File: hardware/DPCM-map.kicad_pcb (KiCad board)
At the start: 2 copper layers, 180 x 180 mm, 1 part

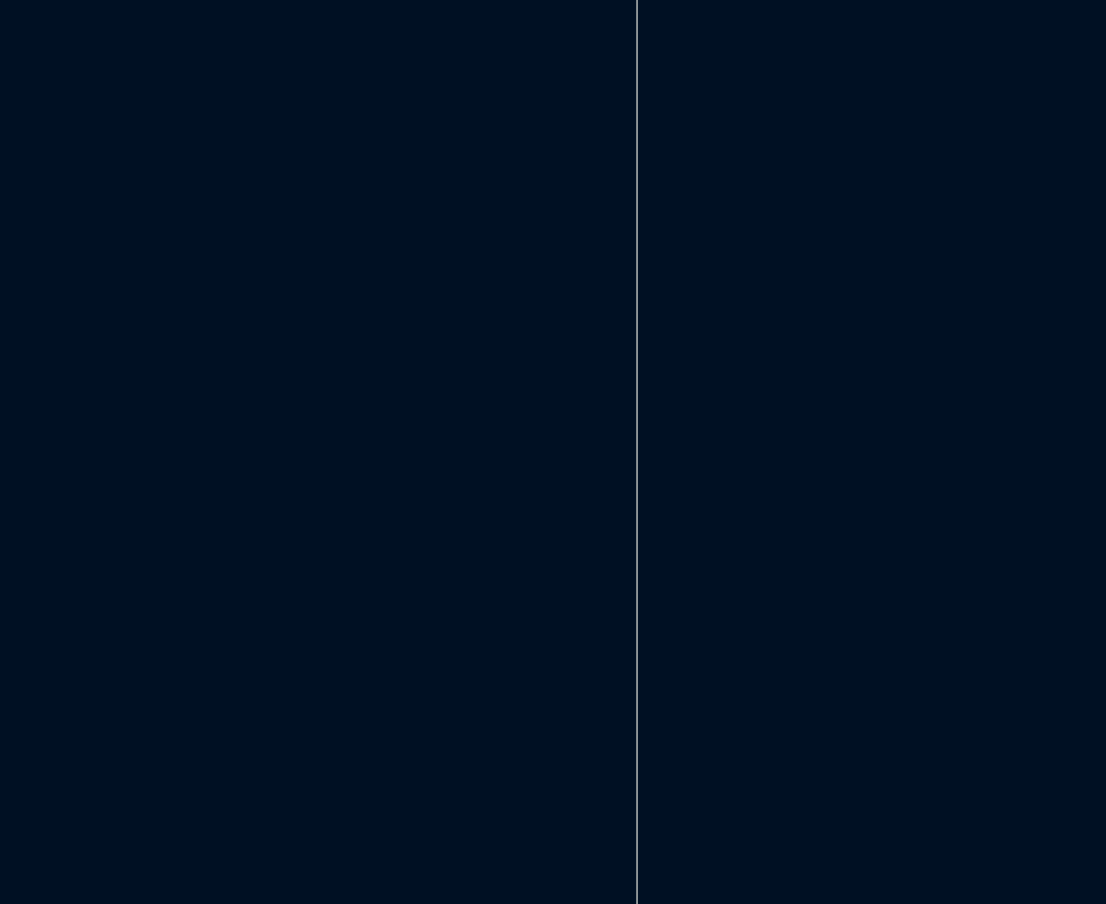
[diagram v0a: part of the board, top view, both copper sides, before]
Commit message: minor changes to pcb: added led footprint for comparison
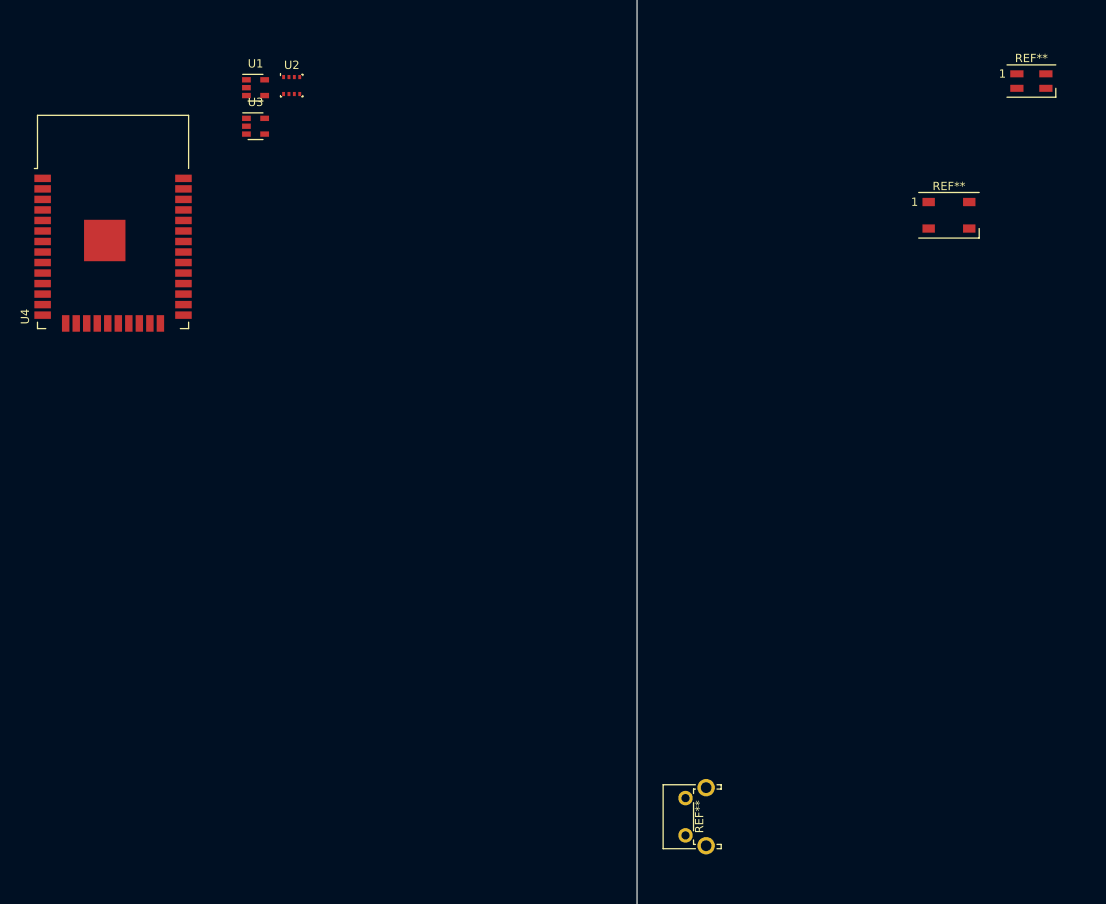
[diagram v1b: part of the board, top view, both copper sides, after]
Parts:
- added REF**: SW_Tactile_SPST_Angled_PTS645Vx39-2LFS, Button_Switch_THT:SW_Tactile_SPST_Angled_PTS645Vx39-2LFS, F.Cu at (5.85, 141.1)
- added REF**: LED_SK6812MINI_PLCC4_3.5x3.5mm_P1.75mm, LED_SMD:LED_SK6812MINI_PLCC4_3.5x3.5mm_P1.75mm, F.Cu at (47.6, 50.0)
- added REF**: LED_WS2812B_PLCC4_5.0x5.0mm_P3.2mm, LED_SMD:LED_WS2812B_PLCC4_5.0x5.0mm_P3.2mm, F.Cu at (37.6, 66.2)
- added U1: TLV75533PDBV, Package_TO_SOT_SMD:SOT-23-5, F.Cu at (-46.0, 50.9)
- added U2: BME280, Package_LGA:Bosch_LGA-8_2.5x2.5mm_P0.65mm_ClockwisePinNumbering, F.Cu at (-41.7, 50.6)
- added U3: MCP73811T, Package_TO_SOT_SMD:SOT-23-5, F.Cu at (-46.0, 55.5)
- added U4: ESP32-WROOM-32, RF_Module:ESP32-WROOM-32, F.Cu at (-63.2, 70.0)

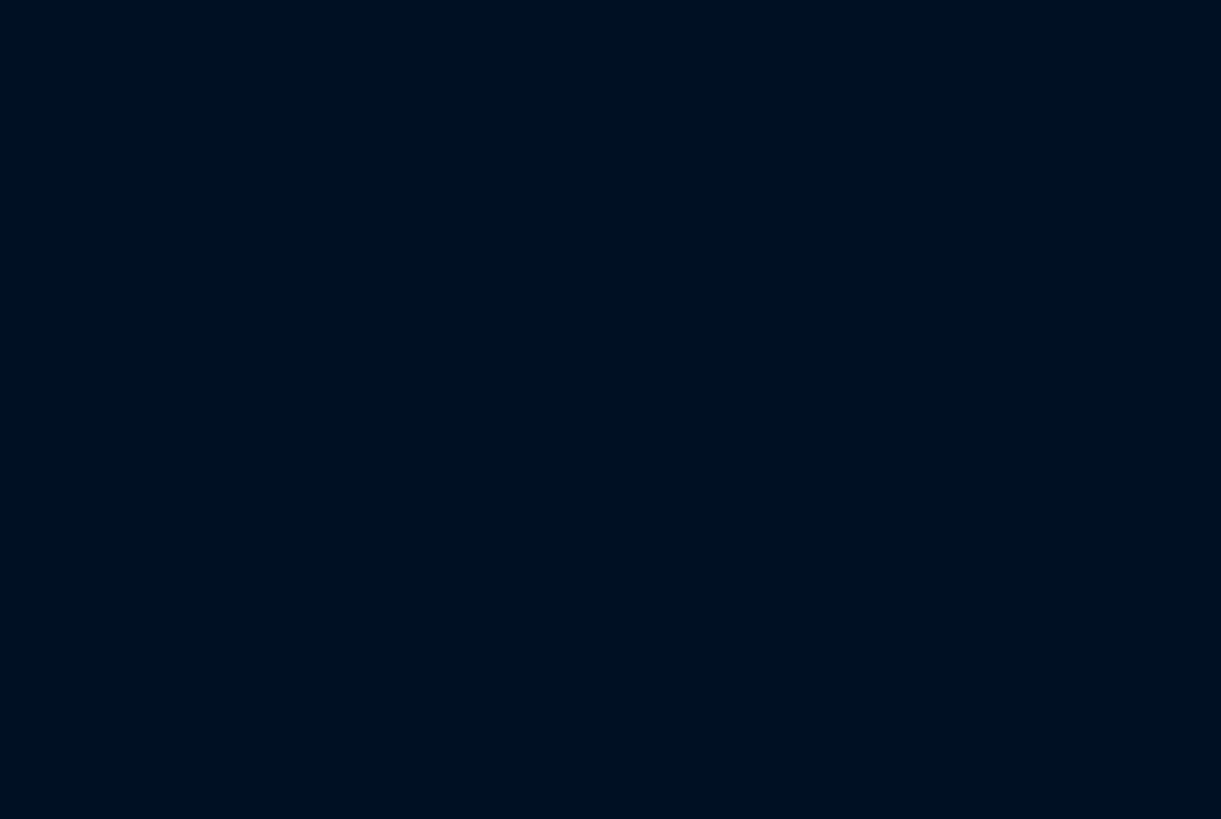
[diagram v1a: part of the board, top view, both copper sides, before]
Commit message: add LCSC ref
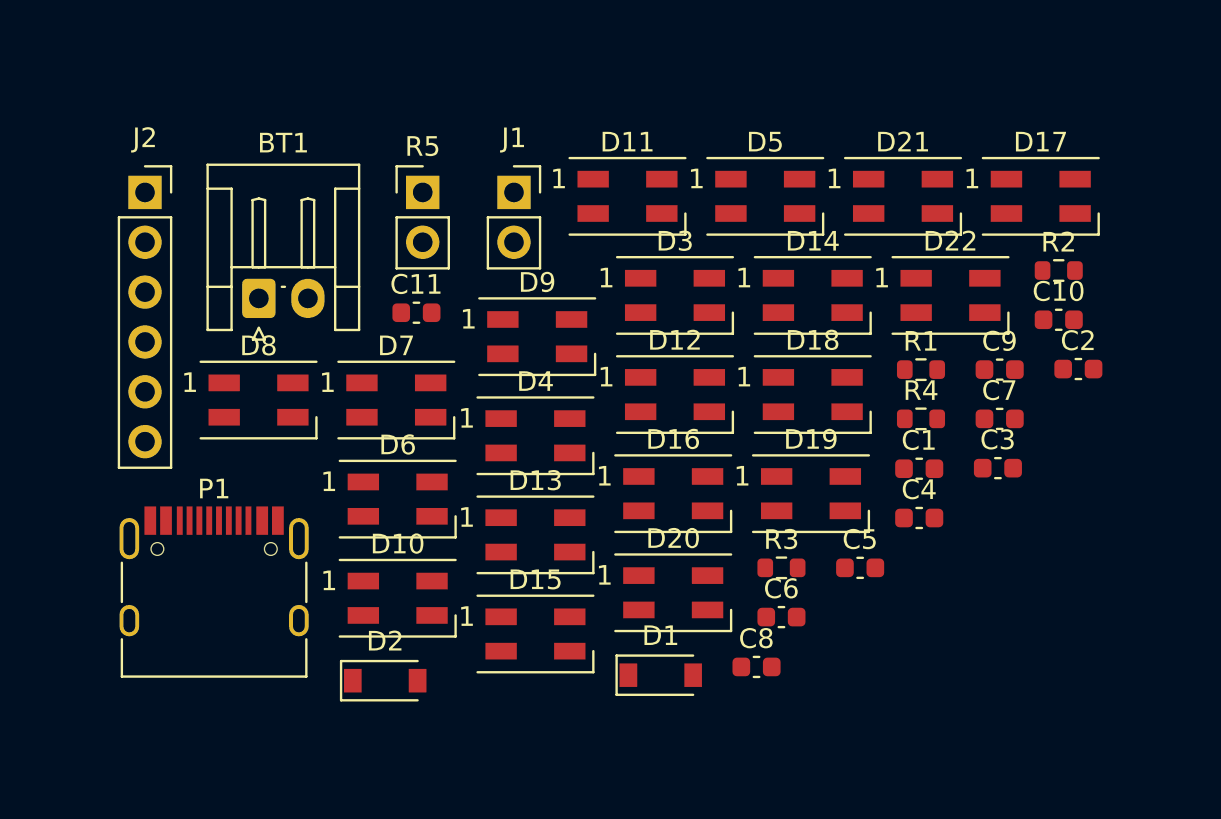
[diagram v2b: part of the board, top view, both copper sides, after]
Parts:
- added BT1: Battery_Cell, Connector_JST:JST_EH_S2B-EH_1x02_P2.50mm_Horizontal, F.Cu at (-52.4, 15.3)
- added C1: 10u, Capacitor_SMD:C_0603_1608Metric, F.Cu at (-18.7, 24.0)
- added C10: 10u, Capacitor_SMD:C_0603_1608Metric, F.Cu at (-11.6, 16.4)
- added C11: 0.1u, Capacitor_SMD:C_0603_1608Metric, F.Cu at (-44.4, 16.0)
- added C2: 1u, Capacitor_SMD:C_0603_1608Metric, F.Cu at (-10.6, 18.9)
- added C3: 10u, Capacitor_SMD:C_0603_1608Metric, F.Cu at (-14.7, 23.9)
- added C4: 0.1u, Capacitor_SMD:C_0603_1608Metric, F.Cu at (-18.7, 26.5)
- added C5: 10u, Capacitor_SMD:C_0603_1608Metric, F.Cu at (-21.8, 29.0)
- added C6: 10u, Capacitor_SMD:C_0603_1608Metric, F.Cu at (-25.8, 31.5)
- added C7: 0.1u, Capacitor_SMD:C_0603_1608Metric, F.Cu at (-14.6, 21.4)
- added C8: 10u, Capacitor_SMD:C_0603_1608Metric, F.Cu at (-27.0, 34.1)
- added C9: 10u, Capacitor_SMD:C_0603_1608Metric, F.Cu at (-14.6, 18.9)
- added D1: 1N5819, Diode_SMD:D_SOD-123, F.Cu at (-31.9, 34.5)
- added D10: WS2812B, LED_SMD:LED_SK6812MINI_PLCC4_3.5x3.5mm_P1.75mm, F.Cu at (-45.3, 30.6)
- added D11: WS2812B, LED_SMD:LED_SK6812MINI_PLCC4_3.5x3.5mm_P1.75mm, F.Cu at (-33.6, 10.1)
- added D12: WS2812B, LED_SMD:LED_SK6812MINI_PLCC4_3.5x3.5mm_P1.75mm, F.Cu at (-31.2, 20.2)
- added D13: WS2812B, LED_SMD:LED_SK6812MINI_PLCC4_3.5x3.5mm_P1.75mm, F.Cu at (-38.3, 27.4)
- added D14: WS2812B, LED_SMD:LED_SK6812MINI_PLCC4_3.5x3.5mm_P1.75mm, F.Cu at (-24.2, 15.2)
- added D15: WS2812B, LED_SMD:LED_SK6812MINI_PLCC4_3.5x3.5mm_P1.75mm, F.Cu at (-38.3, 32.4)
- added D16: WS2812B, LED_SMD:LED_SK6812MINI_PLCC4_3.5x3.5mm_P1.75mm, F.Cu at (-31.3, 25.2)
- added D17: WS2812B, LED_SMD:LED_SK6812MINI_PLCC4_3.5x3.5mm_P1.75mm, F.Cu at (-12.5, 10.1)
- added D18: WS2812B, LED_SMD:LED_SK6812MINI_PLCC4_3.5x3.5mm_P1.75mm, F.Cu at (-24.2, 20.2)
- added D19: WS2812B, LED_SMD:LED_SK6812MINI_PLCC4_3.5x3.5mm_P1.75mm, F.Cu at (-24.3, 25.2)
- added D2: 1N5819, Diode_SMD:D_SOD-123, F.Cu at (-46.0, 34.8)
- added D20: WS2812B, LED_SMD:LED_SK6812MINI_PLCC4_3.5x3.5mm_P1.75mm, F.Cu at (-31.3, 30.3)
- added D21: WS2812B, LED_SMD:LED_SK6812MINI_PLCC4_3.5x3.5mm_P1.75mm, F.Cu at (-19.6, 10.1)
- added D22: WS2812B, LED_SMD:LED_SK6812MINI_PLCC4_3.5x3.5mm_P1.75mm, F.Cu at (-17.1, 15.2)
- added D3: WS2812B, LED_SMD:LED_SK6812MINI_PLCC4_3.5x3.5mm_P1.75mm, F.Cu at (-31.2, 15.2)
- added D4: WS2812B, LED_SMD:LED_SK6812MINI_PLCC4_3.5x3.5mm_P1.75mm, F.Cu at (-38.3, 22.3)
- added D5: WS2812B, LED_SMD:LED_SK6812MINI_PLCC4_3.5x3.5mm_P1.75mm, F.Cu at (-26.6, 10.1)
- added D6: WS2812B, LED_SMD:LED_SK6812MINI_PLCC4_3.5x3.5mm_P1.75mm, F.Cu at (-45.3, 25.5)
- added D7: WS2812B, LED_SMD:LED_SK6812MINI_PLCC4_3.5x3.5mm_P1.75mm, F.Cu at (-45.4, 20.5)
- added D8: WS2812B, LED_SMD:LED_SK6812MINI_PLCC4_3.5x3.5mm_P1.75mm, F.Cu at (-52.4, 20.5)
- added D9: WS2812B, LED_SMD:LED_SK6812MINI_PLCC4_3.5x3.5mm_P1.75mm, F.Cu at (-38.2, 17.2)
- added J1: Conn_01x02_Male, Connector_PinSocket_2.54mm:PinSocket_1x02_P2.54mm_Vertical, F.Cu at (-39.4, 9.90)
- added J2: Conn_01x06_Male, Connector_PinSocket_2.54mm:PinSocket_1x06_P2.54mm_Vertical, F.Cu at (-58.2, 9.90)
- added P1: USB_C_Plug, Connector_USB:USB_C_Receptacle_HRO_TYPE-C-31-M-12, F.Cu at (-54.7, 30.7)
- added R1: 10k, Resistor_SMD:R_0603_1608Metric, F.Cu at (-18.6, 18.9)
- added R2: 10k, Resistor_SMD:R_0603_1608Metric, F.Cu at (-11.6, 13.9)
- added R3: 10k, Resistor_SMD:R_0603_1608Metric, F.Cu at (-25.8, 29.0)
- added R4: 10k, Resistor_SMD:R_0603_1608Metric, F.Cu at (-18.6, 21.4)
- added R5: LDR, Connector_PinHeader_2.54mm:PinHeader_1x02_P2.54mm_Vertical, F.Cu at (-44.0, 9.90)
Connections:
- U1 pad 4: Net-(U1-Pad4) -> (no net)
- U4 pad 10: Net-(U4-Pad10) -> (no net)
- U4 pad 11: Net-(U4-Pad11) -> (no net)
- U4 pad 12: Net-(U4-Pad12) -> (no net)
- U4 pad 13: Net-(U4-Pad13) -> (no net)
- U4 pad 14: Net-(U4-Pad14) -> (no net)
- U4 pad 16: Net-(U4-Pad16) -> (no net)
- U4 pad 17: Net-(U4-Pad17) -> (no net)
- U4 pad 18: Net-(U4-Pad18) -> (no net)
- U4 pad 19: Net-(U4-Pad19) -> (no net)
- U4 pad 20: Net-(U4-Pad20) -> (no net)
- U4 pad 21: Net-(U4-Pad21) -> (no net)
- U4 pad 22: Net-(U4-Pad22) -> (no net)
- U4 pad 24: Net-(U4-Pad24) -> (no net)
- U4 pad 25: Net-(U4-Pad25) -> (no net)
- U4 pad 26: Net-(U4-Pad26) -> (no net)
- U4 pad 27: Net-(U4-Pad27) -> (no net)
- U4 pad 28: Net-(U4-Pad28) -> (no net)
- U4 pad 29: Net-(U4-Pad29) -> (no net)
- U4 pad 30: Net-(U4-Pad30) -> (no net)
- U4 pad 31: Net-(U4-Pad31) -> (no net)
- U4 pad 32: Net-(U4-Pad32) -> (no net)
- U4 pad 37: Net-(U4-Pad37) -> (no net)
- U4 pad 4: Net-(U4-Pad4) -> (no net)
- U4 pad 5: Net-(U4-Pad5) -> (no net)
- U4 pad 6: Net-(U4-Pad6) -> (no net)
- U4 pad 8: Net-(U4-Pad8) -> (no net)
- U4 pad 9: Net-(U4-Pad9) -> (no net)

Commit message: add graphics,edges,keepout
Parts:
- removed the G*** at (180.0, 180.0)
- added G***: LOGO, map_edges_keepout:maps_edges_keepout, F.Cu at (288.8, 226.4)
- added REF**: MountingHole_4mm, MountingHole:MountingHole_4mm, F.Cu at (120.6, 58.5)
- added REF**: MountingHole_4mm, MountingHole:MountingHole_4mm, F.Cu at (120.6, 216.9)
- added REF**: MountingHole_4mm, MountingHole:MountingHole_4mm, F.Cu at (279.0, 216.9)
- added REF**: MountingHole_4mm, MountingHole:MountingHole_4mm, F.Cu at (279.0, 58.5)
- moved REF** 159.4 mm to (-77.9, -48.2)
- moved REF** 159.4 mm to (-87.9, -32.0)
- moved REF** 81.1 mm to (-71.2, 115.8)
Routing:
- added copper zone on B.Cu, net GND
- added copper zone on F.Cu, net GND
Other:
- board size 180 x 180 mm -> 177.4 x 177.4 mm

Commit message: cazzo commento a fare che tanto faremo il rebase
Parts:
- removed BT1: Battery_Cell, Connector_JST:JST_EH_S2B-EH_1x02_P2.50mm_Horizontal
- removed C1, C10, C3, C5, C6, C8, C9: 10u, Capacitor_SMD:C_0603_1608Metric
- removed C11, C4, C7: 0.1u, Capacitor_SMD:C_0603_1608Metric
- removed C2: 1u, Capacitor_SMD:C_0603_1608Metric
- removed D1, D2: 1N5819, Diode_SMD:D_SOD-123
- removed D10, D11, D12, D13, D14, D15, D16, D17, D18, D19, D20, D21, D22, D3, D4, D5, D6, D7, D8, D9: WS2812B, LED_SMD:LED_SK6812MINI_PLCC4_3.5x3.5mm_P1.75mm
- removed J1: Conn_01x02_Male, Connector_PinSocket_2.54mm:PinSocket_1x02_P2.54mm_Vertical
- removed J2: Conn_01x06_Male, Connector_PinSocket_2.54mm:PinSocket_1x06_P2.54mm_Vertical
- removed P1: USB_C_Plug, Connector_USB:USB_C_Receptacle_HRO_TYPE-C-31-M-12
- removed R1, R2, R3, R4: 10k, Resistor_SMD:R_0603_1608Metric
- removed R5: LDR, Connector_PinHeader_2.54mm:PinHeader_1x02_P2.54mm_Vertical
- removed the REF** at (-71.2, 115.8)
- removed the REF** at (-77.9, -48.2)
- removed the REF** at (-87.9, -32.0)
- removed U1: TLV75533PDBV, Package_TO_SOT_SMD:SOT-23-5
- removed U2: BME280, Package_LGA:Bosch_LGA-8_2.5x2.5mm_P0.65mm_ClockwisePinNumbering
- removed U3: MCP73811T, Package_TO_SOT_SMD:SOT-23-5
- removed U4: ESP32-WROOM-32, RF_Module:ESP32-WROOM-32

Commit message: first layout draft
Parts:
- removed the REF** at (120.6, 216.9)
- removed the REF** at (279.0, 216.9)
- removed the REF** at (279.0, 58.5)
- added C1: 10u, Capacitor_SMD:C_0603_1608Metric, F.Cu at (274.6, 123.4)
- added C10: 10u, Capacitor_SMD:C_0603_1608Metric, F.Cu at (273.5, 70.4)
- added C11: 100n, Capacitor_SMD:C_0603_1608Metric, F.Cu at (273.5, 73.6)
- added C12: 100n, Capacitor_SMD:C_0603_1608Metric, F.Cu at (268.8, 132.3)
- added C13: 100n, Capacitor_SMD:C_0603_1608Metric, F.Cu at (196.7, 122.6)
- added C14: 100n, Capacitor_SMD:C_0603_1608Metric, F.Cu at (273.5, 75.2)
- added C15: 18p, Capacitor_SMD:C_0805_2012Metric, F.Cu at (250.4, 110.9)
- added C16: 18p, Capacitor_SMD:C_0805_2012Metric, F.Cu at (249.6, 116.5)
- added C17: 10u, Capacitor_SMD:C_0603_1608Metric, F.Cu at (269.2, 116.0)
- added C18: 10u, Capacitor_SMD:C_0603_1608Metric, F.Cu at (255.3, 106.2)
- added C19: 100n, Capacitor_SMD:C_0603_1608Metric, F.Cu at (258.4, 106.2)
- added C2: 1u, Capacitor_SMD:C_0603_1608Metric, F.Cu at (277.2, 191.2)
- added C20: 100n, Capacitor_SMD:C_0603_1608Metric, F.Cu at (255.3, 104.6)
- added C21: 100n, Capacitor_SMD:C_0603_1608Metric, F.Cu at (189.6, 80.2)
- added C22: 100n, Capacitor_SMD:C_0603_1608Metric, F.Cu at (203.2, 72.2)
- added C23: 100n, Capacitor_SMD:C_0603_1608Metric, F.Cu at (183.0, 67.3)
- added C24: 100n, Capacitor_SMD:C_0603_1608Metric, F.Cu at (180.1, 97.0)
- added C25: 100n, Capacitor_SMD:C_0603_1608Metric, F.Cu at (237.9, 160.4)
- added C26: 100n, Capacitor_SMD:C_0603_1608Metric, F.Cu at (232.3, 145.6)
- added C27: 100n, Capacitor_SMD:C_0603_1608Metric, F.Cu at (213.9, 203.8)
- added C28: 100n, Capacitor_SMD:C_0603_1608Metric, F.Cu at (205.3, 116.3)
- added C29: 100n, Capacitor_SMD:C_0603_1608Metric, F.Cu at (274.6, 121.8)
- added C3: 10u, Capacitor_SMD:C_0603_1608Metric, F.Cu at (143.9, 90.9)
- added C30: 100n, Capacitor_SMD:C_0603_1608Metric, F.Cu at (181.6, 114.6)
- added C31: 100n, Capacitor_SMD:C_0603_1608Metric, F.Cu at (146.9, 103.9)
- added C32: 100n, Capacitor_SMD:C_0603_1608Metric, F.Cu at (160.9, 100.4)
- added C33: 100n, Capacitor_SMD:C_0603_1608Metric, F.Cu at (135.9, 81.6)
- added C34: 100n, Capacitor_SMD:C_0603_1608Metric, F.Cu at (274.6, 120.2)
- added C35: 100n, Capacitor_SMD:C_0603_1608Metric, F.Cu at (165.3, 80.2)
- added C36: 100n, Capacitor_SMD:C_0603_1608Metric, F.Cu at (242.8, 181.6)
- added C37: 100n, Capacitor_SMD:C_0603_1608Metric, F.Cu at (157.4, 167.5)
- added C38: 100n, Capacitor_SMD:C_0603_1608Metric, F.Cu at (218.7, 145.8)
- added C39: 100n, Capacitor_SMD:C_0603_1608Metric, F.Cu at (198.6, 139.1)
- added C4: 100n, Capacitor_SMD:C_0603_1608Metric, F.Cu at (277.2, 192.9)
- added C40: 100n, Capacitor_SMD:C_0603_1608Metric, F.Cu at (223.8, 153.5)
- added C5: 10u, Capacitor_SMD:C_0603_1608Metric, F.Cu at (268.8, 123.4)
- added C6: 10u, Capacitor_SMD:C_0603_1608Metric, F.Cu at (254.2, 159.5)
- added C7: 100n, Capacitor_SMD:C_0603_1608Metric, F.Cu at (269.2, 109.7)
- added C8: 10u, Capacitor_SMD:C_0603_1608Metric, F.Cu at (212.7, 133.1)
- added C9: 10u, Capacitor_SMD:C_0603_1608Metric, F.Cu at (273.5, 72.0)
- added D1: WS2812B, LED_SMD:LED_SK6812MINI_PLCC4_3.5x3.5mm_P1.75mm, F.Cu at (215.2, 206.7)
- added D10: WS2812B, LED_SMD:LED_SK6812MINI_PLCC4_3.5x3.5mm_P1.75mm, F.Cu at (255.9, 162.6)
- added D11: WS2812B, LED_SMD:LED_SK6812MINI_PLCC4_3.5x3.5mm_P1.75mm, F.Cu at (145.3, 94.1)
- added D12: WS2812B, LED_SMD:LED_SK6812MINI_PLCC4_3.5x3.5mm_P1.75mm, F.Cu at (239.4, 163.4)
- added D13: WS2812B, LED_SMD:LED_SK6812MINI_PLCC4_3.5x3.5mm_P1.75mm, F.Cu at (139.6, 81.6)
- added D14: WS2812B, LED_SMD:LED_SK6812MINI_PLCC4_3.5x3.5mm_P1.75mm, F.Cu at (148.2, 106.9)
- added D15: WS2812B, LED_SMD:LED_SK6812MINI_PLCC4_3.5x3.5mm_P1.75mm, F.Cu at (162.5, 103.3)
- added D16: WS2812B, LED_SMD:LED_SK6812MINI_PLCC4_3.5x3.5mm_P1.75mm, F.Cu at (181.4, 100.0)
- added D17: WS2812B, LED_SMD:LED_SK6812MINI_PLCC4_3.5x3.5mm_P1.75mm, F.Cu at (182.9, 117.4)
- added D18: WS2812B, LED_SMD:LED_SK6812MINI_PLCC4_3.5x3.5mm_P1.75mm, F.Cu at (206.6, 119.3)
- added D19: WS2812B, LED_SMD:LED_SK6812MINI_PLCC4_3.5x3.5mm_P1.75mm, F.Cu at (198.1, 125.6)
- added D2: WS2812B, LED_SMD:LED_SK6812MINI_PLCC4_3.5x3.5mm_P1.75mm, F.Cu at (244.1, 184.5)
- added D20: WS2812B, LED_SMD:LED_SK6812MINI_PLCC4_3.5x3.5mm_P1.75mm, F.Cu at (214.2, 136.1)
- added D21: WS2812B, LED_SMD:LED_SK6812MINI_PLCC4_3.5x3.5mm_P1.75mm, F.Cu at (199.9, 141.9)
- added D22: WS2812B, LED_SMD:LED_SK6812MINI_PLCC4_3.5x3.5mm_P1.75mm, F.Cu at (158.9, 170.5)
- added D23: 1N4148W, Diode_SMD:D_SOD-123, F.Cu at (218.8, 72.3)
- added D3: WS2812B, LED_SMD:LED_SK6812MINI_PLCC4_3.5x3.5mm_P1.75mm, F.Cu at (190.9, 83.1)
- added D4: WS2812B, LED_SMD:LED_SK6812MINI_PLCC4_3.5x3.5mm_P1.75mm, F.Cu at (225.1, 156.4)
- added D5: WS2812B, LED_SMD:LED_SK6812MINI_PLCC4_3.5x3.5mm_P1.75mm, F.Cu at (204.5, 75.1)
- added D6: WS2812B, LED_SMD:LED_SK6812MINI_PLCC4_3.5x3.5mm_P1.75mm, F.Cu at (222.4, 145.6)
- added D7: WS2812B, LED_SMD:LED_SK6812MINI_PLCC4_3.5x3.5mm_P1.75mm, F.Cu at (184.3, 70.1)
- added D8: WS2812B, LED_SMD:LED_SK6812MINI_PLCC4_3.5x3.5mm_P1.75mm, F.Cu at (233.7, 148.6)
- added D9: WS2812B, LED_SMD:LED_SK6812MINI_PLCC4_3.5x3.5mm_P1.75mm, F.Cu at (166.6, 83.0)
- added J1: JMP, Connector_PinSocket_2.54mm:PinSocket_1x02_P2.54mm_Vertical, F.Cu at (271.9, 106.9)
- added J2: Conn_01x06_Male, Connector_PinSocket_2.54mm:PinSocket_1x06_P2.54mm_Vertical, F.Cu at (258.5, 99.2)
- added J3: Touch_Pad_-, Connector_Wire:SolderWire-0.75sqmm_1x01_D1.25mm_OD2.3mm, F.Cu at (143.1, 58.4)
- added J4: Touch_Pad_0, Connector_Wire:SolderWire-0.75sqmm_1x01_D1.25mm_OD2.3mm, F.Cu at (143.1, 63.0)
- added J5: Touch_Pad_+, Connector_Wire:SolderWire-0.75sqmm_1x01_D1.25mm_OD2.3mm, F.Cu at (143.1, 67.9)
- added J6: JMP, Connector_PinSocket_2.54mm:PinSocket_1x02_P2.54mm_Vertical, F.Cu at (271.9, 113.1)
- added J7: SSD1306, Connector_PinHeader_2.54mm:PinHeader_1x04_P2.54mm_Vertical, F.Cu at (127.7, 110.8)
- added JP1: SolderJumper_3_Open, Jumper:SolderJumper-3_P1.3mm_Open_RoundedPad1.0x1.5mm_NumberLabels, F.Cu at (143.2, 118.8)
- added JP2: Jumper, Jumper:SolderJumper-2_P1.3mm_Bridged_RoundedPad1.0x1.5mm, F.Cu at (219.0, 74.8)
- added JP3: SolderJumper_3_Open, Jumper:SolderJumper-3_P1.3mm_Open_RoundedPad1.0x1.5mm_NumberLabels, F.Cu at (147.2, 118.6)
- added P1: USB_C_Plug, Connector_USB:USB_C_Receptacle_HRO_TYPE-C-31-M-12, F.Cu at (284.3, 126.8)
- added Q1: 2N7002, Package_TO_SOT_SMD:SOT-23, F.Cu at (262.5, 108.8)
- added Q2: 2N7002, Package_TO_SOT_SMD:SOT-23, F.Cu at (262.5, 115.6)
- added R1: 10k, Resistor_SMD:R_0603_1608Metric, F.Cu at (277.2, 199.4)
- added R2: 10k, Resistor_SMD:R_0603_1608Metric, F.Cu at (277.2, 197.7)
- added R3: 10k, Resistor_SMD:R_0603_1608Metric, F.Cu at (269.2, 106.6)
- added R4: 10k, Resistor_SMD:R_0603_1608Metric, F.Cu at (263.4, 59.4)
- added R5: LDR, Connector_PinHeader_2.54mm:PinHeader_1x02_P2.54mm_Vertical, F.Cu at (263.1, 65.5)
- added R6: 10k, Resistor_SMD:R_0603_1608Metric, F.Cu at (269.2, 112.8)
- added R7: 10k, Resistor_SMD:R_0603_1608Metric, F.Cu at (262.7, 113.0)
- added R8: 10k, Resistor_SMD:R_0603_1608Metric, F.Cu at (262.7, 111.4)
- added REF**: MountingHole_4mm, MountingHole:MountingHole_4mm, F.Cu at (120.5, 218.0)
- added REF**: MountingHole_4mm, MountingHole:MountingHole_4mm, F.Cu at (278.5, 218.0)
- added REF**: MountingHole_4mm, MountingHole:MountingHole_4mm, F.Cu at (278.5, 60.0)
- added SW1: SW_Push, Button_Switch_THT:SW_Tactile_SPST_Angled_PTS645Vx58-2LFS, F.Cu at (285.3, 108.1)
- added SW2: SW_+_Fb, Button_Switch_THT:SW_Tactile_SPST_Angled_PTS645Vx58-2LFS, F.Cu at (223.0, 54.0)
- added SW3: SW_0_Fb, Button_Switch_THT:SW_Tactile_SPST_Angled_PTS645Vx58-2LFS, F.Cu at (249.0, 54.0)
- added SW4: SW_-_Fb, Button_Switch_THT:SW_Tactile_SPST_Angled_PTS645Vx58-2LFS, F.Cu at (236.0, 54.0)
- added U1: AZ1117-3.3, Package_TO_SOT_SMD:SOT-223-3_TabPin2, F.Cu at (271.8, 127.9)
- added U2: BME280, Package_LGA:Bosch_LGA-8_2.5x2.5mm_P0.65mm_ClockwisePinNumbering, F.Cu at (277.3, 195.4)
- added U4: ESP32-WROOM-32, RF_Module:ESP32-WROOM-32, F.Cu at (265.9, 85.8)
- added U5: CH340G, Package_SO:SOIC-16_3.9x9.9mm_P1.27mm, F.Cu at (256.3, 112.2)
- added Y1: 12MHz, Crystal:Crystal_SMD_3225-4Pin_3.2x2.5mm, F.Cu at (250.0, 113.7)
- moved G*** 4.15 mm to (285.5, 223.9)
- moved REF** 1.59 mm to (120.5, 60.0)
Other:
- board size 177.4 x 177.4 mm -> 178 x 178 mm
